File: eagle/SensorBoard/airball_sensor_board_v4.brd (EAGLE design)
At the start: 139.7 x 38.1 mm, 66 parts, among them J2 AVR_SPI_PROG_3X2PTH, U2 MCP73831, U3 MIC5219 3.3V, Y1 8MHz

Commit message: Add newest WIP for airball_sensor_board_v4 and STL
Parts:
- removed U$1: 32U4, jcole:TQFP44
- removed U$2: DS2782, airball:TSSOP8
- removed U1: (no value), airball:TSSOP24
- removed U2: MCP73831, SparkFun-IC-Power:SOT23-5
- removed U3: MIC5219 3.3V, SparkFun-IC-Power:SOT23-5
- removed XB1: XBEE-PRO-SMD, airball:XBEE-PRO-SMD
- added BM: DS2782, airball:TSSOP8
- added C16: 10uF, SparkFun-Capacitors:0603-POLAR
- added CC: MCP73831, SparkFun-IC-Power:SOT23-5
- added D7: (no value), SparkFun-LED:LED-0603
- added F2: 6V/0.5A, SparkFun-Fuses:1206
- added MCU: 32U4, jcole:TQFP44
- added MUX: (no value), airball:TSSOP24
- added VREG: LT1963, airball:SOT223-3
- added XBEE: XBEE-PRO-SMD, airball:XBEE-PRO-SMD
- OAT: value TMP102 -> TMP275; device SparkFun-Sensors:SOT563 -> airball:SOIC8
- R13: device SparkFun-Resistors:0603 -> SparkFun-Resistors:1206
- moved J2 69.0 mm to (99.4, 25.7)
- moved R17 61.8 mm to (96.2, 22.2), turned to 270 degrees
- moved C5 60.6 mm to (88.3, 5.71), turned to 180 degrees
- moved R16 59.1 mm to (93.7, 22.2), turned to 270 degrees
- moved C15 50.7 mm to (94.0, 35.9), turned to 270 degrees
- moved F1 48.8 mm to (130.2, 25.7)
- moved R13 41.5 mm to (125.4, 21.3)
- moved R23 40.6 mm to (84.1, 21.6), turned to 180 degrees
- moved C13 40.5 mm to (79.7, 35.9), turned to 270 degrees
- moved C12 39.9 mm to (79.7, 30.2), turned to 270 degrees
- moved R15 39.8 mm to (120.3, 30.5), turned to 90 degrees
- moved C11 39.1 mm to (83.5, 18.7), turned to 270 degrees
- moved Y1 38.1 mm to (87.9, 18.7)
- moved C10 36.7 mm to (92.4, 18.7), turned to 90 degrees
- moved U$3 35.6 mm to (69.8, 19.1)
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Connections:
- removed net BAT_GND: J1.1, JP1.5, JP1.SH@1, JP1.SH@2, JP1.SH@3, JP1.SH@4, R13.1, R15.1, U$2.2, U2.2
- removed net N$11: R15.2, U2.5
- removed net N$13: R23.2, U$1.13
- removed net N$15: R26.2, XB1.15
- removed net N$17: R27.2, XB1.6
- removed net N$18: R28.2, XB1.13
- removed net N$2: R18.1, U2.1
- removed net N$3: D1.A, J1.2, S1.2, U2.3
- removed net N$4: R11.1, U$2.3
- removed net N$5: R12.1, U$2.4
- removed net N$8: R24.2, U$1.22
- removed net N$9: R25.2, U$1.8
- removed net VCC_5V0_UF: F1.1, JP1.1
- new net ASSOC_LED: R26.2, XBEE.15
- new net BAT+: C16.+, CC.3, D2.A, F2.2, R11.2, R12.2, S1.2
- new net BAT+_UF: F2.1, J1.2
- new net BAT-: BM.2, J1.1, R13.1
- new net BM_VDD: BM.4, R12.1
- new net BM_VIN: BM.3, R11.1
- new net CC_PROG: CC.5, R15.2
- new net CHG_LED: CC.1, R18.1
- new net ON_LED: R28.2, XBEE.13
- new net RSSI_LED: R27.2, XBEE.6
- new net RX_LED: MCU.8, R25.2
- new net TX_LED: MCU.22, R24.2
- net BAT_VRAW: now also VREG.1; no longer R11.2, R12.2, U3.1, U3.3
- net GND: now also BM.7, C16.-, CC.2, D1.A, D7.C, JP1.5, JP1.SH@1, JP1.SH@2, JP1.SH@3, JP1.SH@4, MCU.15, MCU.23, MCU.33, MCU.35, MCU.43, MCU.5, MUX.1, MUX.12, MUX.2, MUX.21, OAT.5, OAT.6, OAT.7, R15.1, VREG.2, VREG.TAB, XBEE.10; no longer D2.C, OAT.2, U$1.15, U$1.23, U$1.33, U$1.35, U$1.43, U$1.5, U$2.7, U1.1, U1.12, U1.2, U1.21, U3.2, XB1.10
- net MISO: now also MCU.11; no longer U$1.11
- net MOSI: now also MCU.10; no longer U$1.10
- net MUX_RST: now also MCU.25, MUX.3; no longer U$1.25, U1.3
- net MUX_SCL: now also MCU.18, MUX.22; no longer U$1.18, U1.22
- net MUX_SDA: now also MCU.19, MUX.23; no longer U$1.19, U1.23
- net N$1: now also D2.C
- net N$10: now also D3.A; no longer D2.A
- net N$12: now also MCU.42; no longer U$1.42
- net N$14: now also D4.A; no longer D3.A
- net N$16: now also MCU.6; no longer U$1.6
- net N$20: now also D5.A; no longer D4.A
- net N$21: now also D6.A; no longer D5.A
- net N$22: now also D7.A; no longer D6.A
- net N$6: now also MCU.17; no longer U$1.17
- net N$7: now also MCU.16; no longer U$1.16
- net RST: now also MCU.13, R23.2
- net RX: now also MCU.20, XBEE.2; no longer U$1.20, XB1.2
- net SCK: now also MCU.9; no longer U$1.9
- net SCL_BARO: now also MUX.7; no longer U1.7
- net SCL_BM: now also BM.6, MUX.20; no longer U$2.6, U1.20
- net SCL_DP0: now also MUX.5; no longer U1.5
- net SCL_DPA: now also MUX.9; no longer U1.9
- net SCL_DPB: now also MUX.11; no longer U1.11
- net SCL_OAT: now also MUX.14, OAT.2; no longer OAT.1, U1.14
- net SDA_BARO: now also MUX.6; no longer U1.6
- net SDA_BM: now also BM.5, MUX.19; no longer U$2.5, U1.19
- net SDA_DP0: now also MUX.4; no longer U1.4
- net SDA_DPA: now also MUX.8; no longer U1.8
- net SDA_DPB: now also MUX.10; no longer U1.10
- net SDA_OAT: now also MUX.13, OAT.1; no longer OAT.6, U1.13
- net TX: now also MCU.21, XBEE.3; no longer U$1.21, XB1.3
- net USB_5V0_UF: now also F1.1, JP1.1; no longer C13.2, U$1.2, U$1.7
- net USB_N: now also MCU.3; no longer U$1.3
- net USB_P: now also MCU.4; no longer U$1.4
- net VCC_3V3: now also MCU.14, MCU.24, MCU.34, MCU.44, MUX.24, OAT.8, VREG.3, XBEE.1; no longer OAT.5, U$1.14, U$1.24, U$1.34, U$1.44, U1.24, U3.5, XB1.1
- net VCC_5V0: now also C13.2, CC.4, MCU.2, MCU.7; no longer U2.4
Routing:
- net VCC_3V3: track 0.00 -> 316.0 mm, vias 0 -> 13
- net ASSOC_LED: track 0.00 -> 117.2 mm, vias 0 -> 1
- net ON_LED: track 0.00 -> 110.4 mm, vias 0 -> 1
- net RSSI_LED: track 0.00 -> 90.7 mm, vias 0 -> 1
- net TX: track 0.00 -> 81.1 mm, vias 0 -> 1
- net SCL_DP0: track 0.00 -> 75.1 mm, vias 0 -> 2
- net RX: track 0.00 -> 73.7 mm, vias 0 -> 1
- net SDA_DP0: track 0.00 -> 71.9 mm, vias 0 -> 3
- net TX_LED: track 0.00 -> 70.7 mm, vias 0 -> 4
- net BAT+: track 0.00 -> 68.4 mm, vias 0 -> 4
- net SCL_BARO: track 0.00 -> 66.4 mm, vias 0 -> 2
- net VCC_5V0: track 0.00 -> 66.4 mm, vias 0 -> 2
- net SDA_BARO: track 0.00 -> 62.3 mm, vias 0 -> 3
- net RX_LED: track 0.00 -> 52.4 mm, vias 0 -> 2
- net USB_N: track 0.00 -> 52.2 mm, vias 0 -> 2
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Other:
- board text added: "2018-02-25"
- board text added: "Airball Sensor v4"
- board text added: "Assoc"
- board text added: "Battery"
- board text added: "Battery Monitor"
- board text added: "Channel 0"
- board text added: "Channel 1"
- board text added: "Channel 2"
- board text added: "Channel 3"
- board text added: "Channel 4"
- board text added: "Channel 7"
- board text added: "Chg."
- board text added: "Designed by Jeremy Cole for Airball.aero Reno, Nevada, USA"
- board text added: "Full"
- board text added: "ICSP"
- board text added: "On"
- board text added: "RSSI"
- board text added: "Rx"
- board text added: "Tx"
- board text added: "USB"
- board text added: "XBee Status"
- board text removed: "2018-02-xx"
- board text removed: "Airball Sensor Board v4"
- board text removed: "Port 0"
- board text removed: "Port 1"
- board text removed: "Port 2"
- board text removed: "Port 3"
- board text removed: "Port 4"
- board text removed: "USB µB"

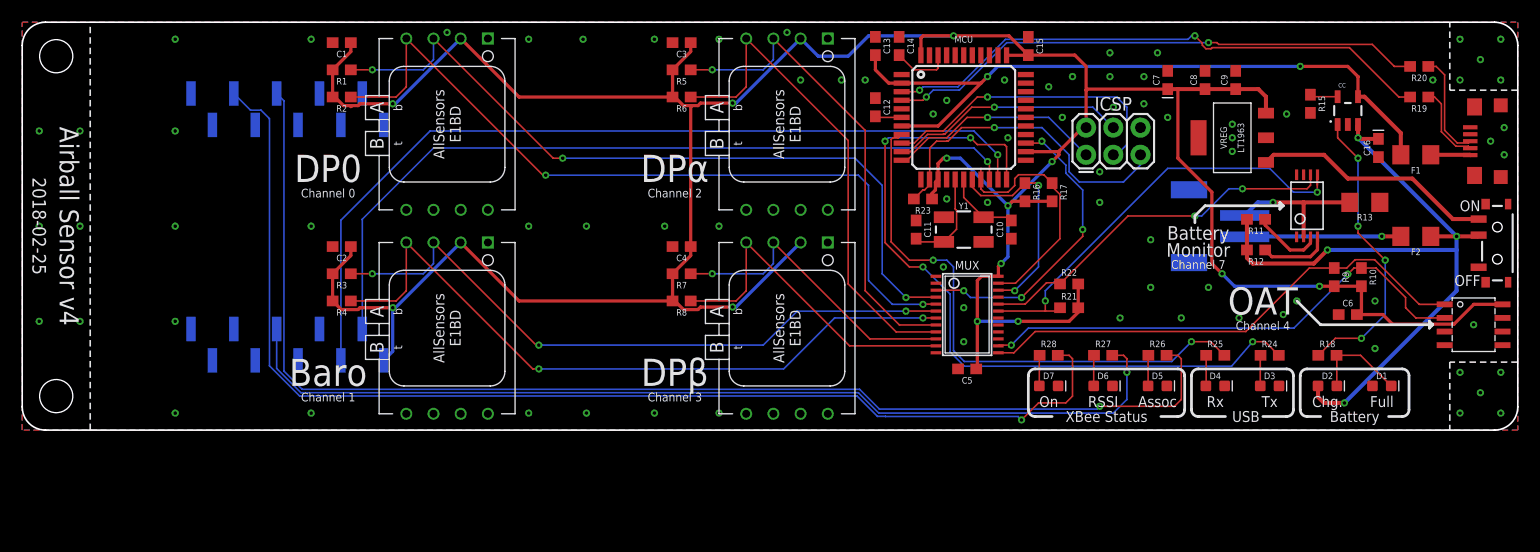
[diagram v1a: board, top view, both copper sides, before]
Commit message: Updated airball_sensor_board_v4 and library; added as-ordered gerbers
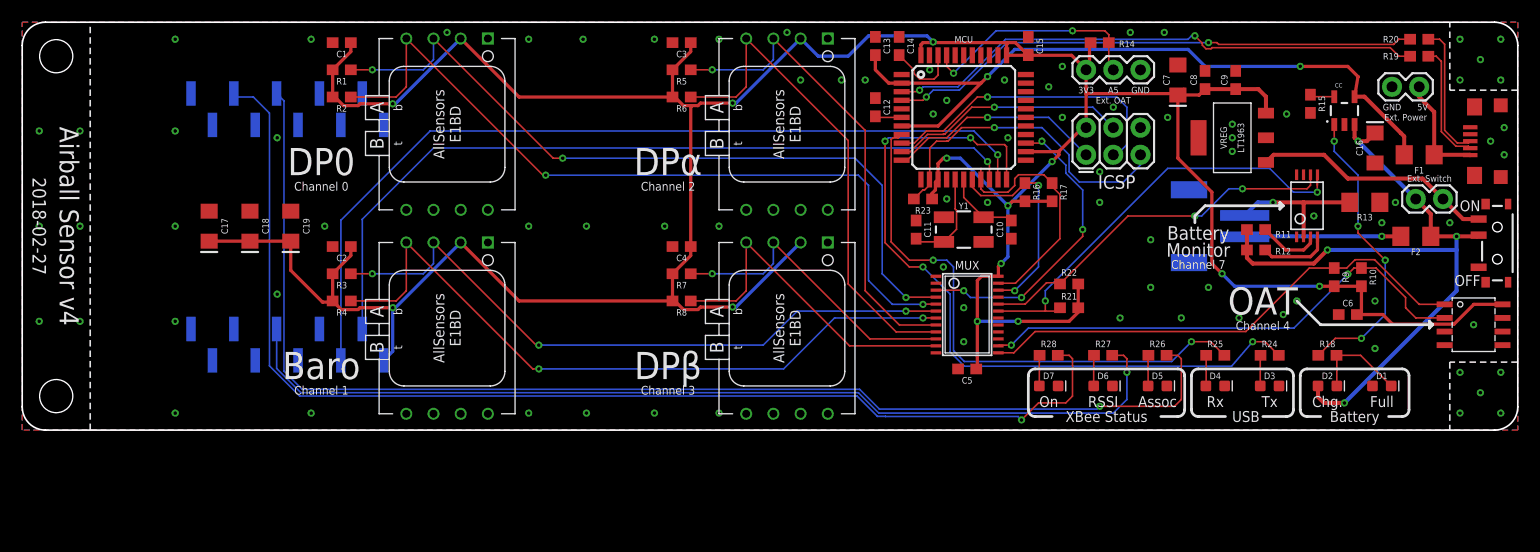
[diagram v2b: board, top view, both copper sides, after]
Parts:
- added C17, C18, C19: 10uF, SparkFun-Capacitors:EIA3216
- added EXT_OAT: (no value), SparkFun-Connectors:1X03
- added EXT_POWER, EXT_SW: (no value), SparkFun-Connectors:1X02
- added R14: 4.7k, SparkFun-Resistors:0603
- C16, C7: device SparkFun-Capacitors:0603-POLAR -> SparkFun-Capacitors:EIA3216
- moved R19 3.81 mm to (130.5, 34.9)
- moved R20 2.54 mm to (130.5, 36.5)
- moved C7 0.95 mm to (108.0, 32.7)
- moved R11 0.95 mm to (115.3, 18.7)
- moved C16 0.32 mm to (126.4, 26.4)
- moved CC 0.32 mm to (123.5, 29.8)
- moved F1 0.32 mm to (130.5, 25.7)
- renumbered J2 to ICSP
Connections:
- net RX renamed RXD
- net TX renamed TXD
- new net EXT_OAT: EXT_OAT.2, MCU.41, R14.1
- net BAT+: now also EXT_SW.1
- net BAT_VRAW: now also EXT_SW.2
- net GND: now also C17.-, C18.-, C19.-, EXT_OAT.3, EXT_POWER.2
- net USB_5V0_UF: now also EXT_POWER.1
- net VCC_3V3: now also C17.+, C18.+, C19.+, EXT_OAT.1, R14.2
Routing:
- net EXT_OAT: track 0.00 -> 21.7 mm, vias 0 -> 2
- net VCC_3V3: track 316.0 -> 334.5 mm
- net USB_5V0_UF: track 3.70 -> 10.3 mm
- net USB_X_N: track 7.42 -> 11.3 mm
- net USB_X_P: track 9.99 -> 12.7 mm
- net BAT+: track 68.4 -> 66.6 mm
- net VCC_5V0: track 66.4 -> 68.2 mm
- net USB_N: track 52.2 -> 50.6 mm
- net N$12: track 5.47 -> 6.76 mm
- net BM_VIN: track 6.58 -> 5.88 mm
- net USB_P: track 50.6 -> 50.0 mm
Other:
- board text added: "2018-02-27"
- board text added: "3V3"
- board text added: "5V"
- board text added: "A5"
- board text added: "Ext. OAT"
- board text added: "Ext. Power"
- board text added: "Ext. Switch"
- board text added: "GND"
- board text removed: "2018-02-25"

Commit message: Minor cleanups to sensor v4
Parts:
- BARO, DP0, DPA, DPB: value ALLSENSORS_DLHR_I2C-E1BD -> (none)
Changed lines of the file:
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@@
 <?xml version="1.0" encoding="utf-8"?>
 <!DOCTYPE eagle SYSTEM "eagle.dtd">
-<eagle version="8.6.3">
+<eagle version="8.7.0">
 <drawing>
 <settings>
-<setting alwaysvectorfont="yes"/>
+<setting alwaysvectorfont="no"/>
 <setting keepoldvectorfont="yes"/>
 <setting verticaltext="up"/>
@@
 <element name="D7" library="SparkFun-LED" package="LED-0603" value="" x="95.885" y="4.1275"/>
 <element name="U$3" library="airball" package="SPARKFUN_LIPO_1000MAH" value="LIPO_BATTERY_OUTLINE-1000MAH" x="69.85" y="19.05" smashed="yes" rot="MR0"/>
-<element name="DP0" library="airball" package="ALLSENSORS_E1BD" value="ALLSENSORS_DLHR_I2C-E1BD" x="39.6875" y="28.575" smashed="yes" rot="R270"/>
-<element name="BARO" library="airball" package="ALLSENSORS_E1BD" value="ALLSENSORS_DLHR_I2C-E1BD" x="39.6875" y="9.525" smashed="yes" rot="R270"/>
-<element name="DPA" library="airball" package="ALLSENSORS_E1BD" value="ALLSENSORS_DLHR_I2C-E1BD" x="71.4375" y="28.575" smashed="yes" rot="R270"/>
-<element name="DPB" library="airball" package="ALLSENSORS_E1BD" value="ALLSENSORS_DLHR_I2C-E1BD" x="71.4375" y="9.525" smashed="yes" rot="R270"/>
+<element name="DP0" library="airball" package="ALLSENSORS_E1BD" value="" x="39.6875" y="28.575" smashed="yes" rot="R270"/>
+<element name="BARO" library="airball" package="ALLSENSORS_E1BD" value="" x="39.6875" y="9.525" smashed="yes" rot="R270"/>
+<element name="DPA" library="airball" package="ALLSENSORS_E1BD" value="" x="71.4375" y="28.575" smashed="yes" rot="R270"/>
+<element name="DPB" library="airball" package="ALLSENSORS_E1BD" value="" x="71.4375" y="9.525" smashed="yes" rot="R270"/>
 <element name="F2" library="SparkFun-Fuses" package="1206" value="6V/0.5A" x="130.175" y="18.0975" smashed="yes">
 <attribute name="NAME" x="130.175" y="16.9545" size="0.6096" layer="21" font="vector" ratio="20" rot="R180" align="bottom-center"/>
@@
 </element>
 <element name="EXT_OAT" library="SparkFun-Connectors" package="1X03" value="" x="99.3775" y="33.655" smashed="yes">
-<attribute name="VALUE" x="98.1075" y="31.623" size="0.6096" layer="27" font="vector" ratio="20"/>
+<attribute name="PROD_ID" value="XXX-00000" x="99.3775" y="33.655" size="1.778" layer="27" display="off"/>
+<attribute name="VALUE" value="455-1750-1-ND" x="98.1075" y="31.623" size="0.6096" layer="27" font="vector" ratio="20"/>
 </element>
 <element name="R14" library="SparkFun-Resistors" package="0603" value="4.7k" x="100.6475" y="36.195" smashed="yes" rot="R180">
